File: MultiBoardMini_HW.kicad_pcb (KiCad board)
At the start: 2 copper layers, 63 x 63 mm, 57 parts, among them J1 PB0, J2 PA10, J3 Conn_01x02_Male, J4 PA10, J6 Conn_01x04, SW1 PF1, SW2 RESET, SW3 SW_Push_DPDT, SW5 SW_Push_DPDT, T3 PTS_1.5_2, U1 M78AR5-1, U2 NUCLEO-F303K8, U3 ESP32-C3-WROOM-02-N4, U4 TB67H303HG, U5 TB67H303HG, U6 MCP2562-E_SN

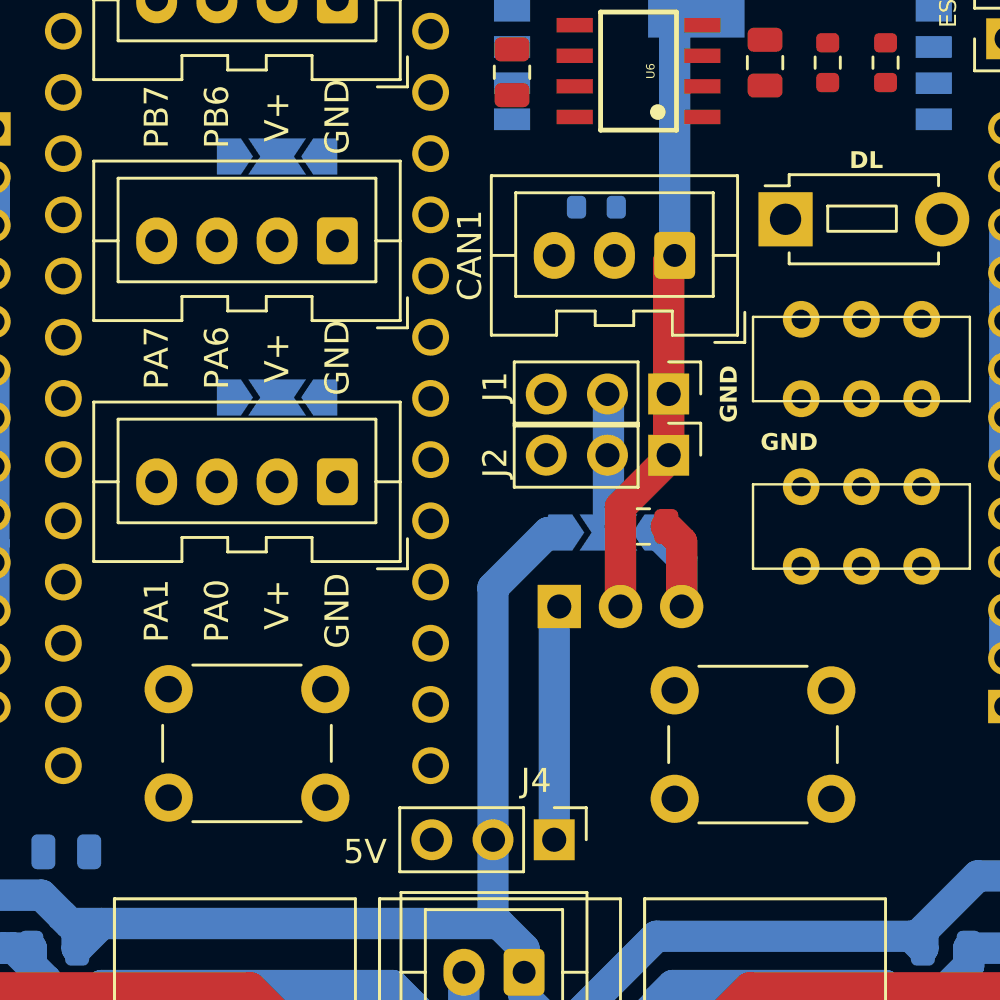
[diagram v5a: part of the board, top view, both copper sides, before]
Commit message: ESP大型化のためつめつめ
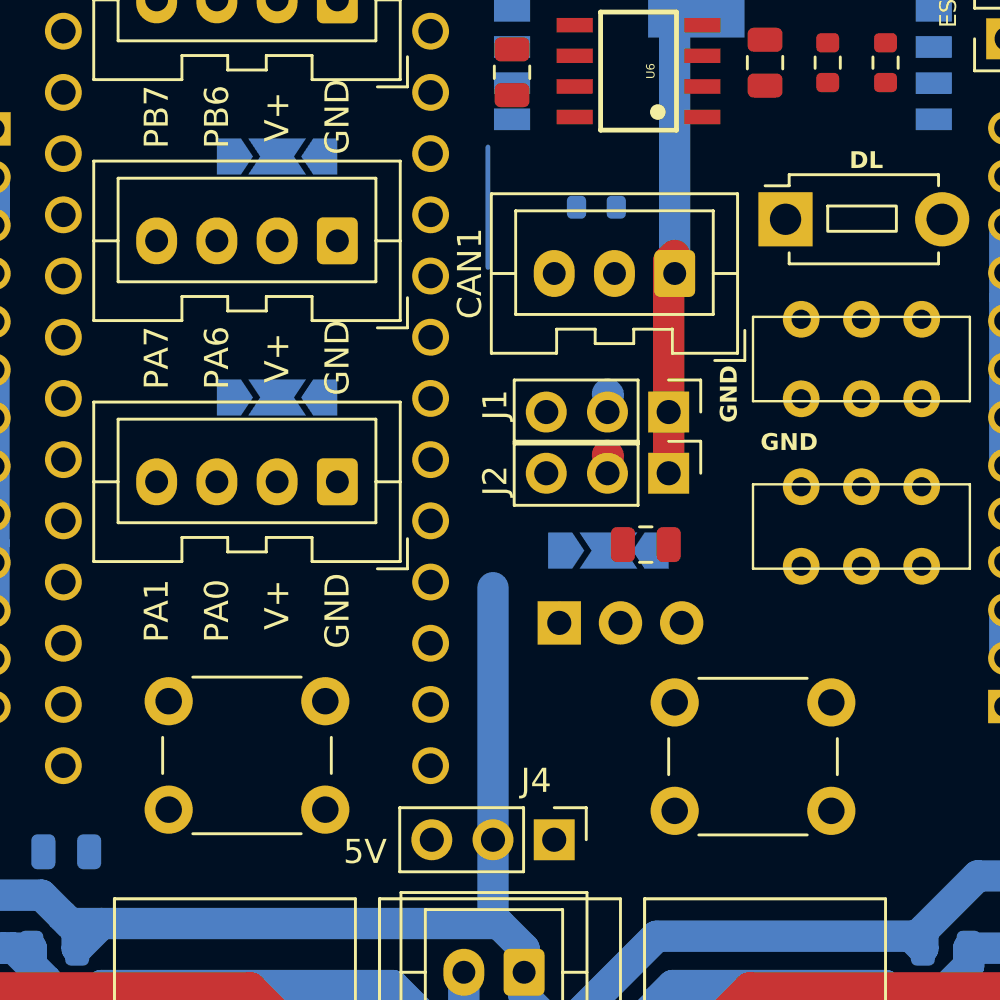
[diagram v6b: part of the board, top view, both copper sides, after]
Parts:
- moved C10 0.76 mm to (6.05, 5.75)
- moved CAN1 0.75 mm to (7.25, -5.50)
- moved J1 0.75 mm to (7.00, 0.25)
- moved J2 0.75 mm to (7.00, 2.79)
- moved JP4 0.75 mm to (4.50, 6.00)
- moved U1 0.68 mm to (5.00, 9.00)
- moved SW1 0.50 mm to (10.5, 14.5)
- moved SW2 0.50 mm to (-10.5, 14.5)
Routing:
- net Net-(J4-Pin_1): track 10.1 -> 0.30 mm
- net +5V: track 7.09 -> 0.00 mm
- net GND: track 182.2 -> 175.3 mm
- net Net-(J1-Pin_2): track 5.82 -> 0.11 mm
- net PWR: track 136.8 -> 133.0 mm
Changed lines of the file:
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@@
   )
   (footprint "Connector_PinHeader_2.54mm:PinHeader_1x03_P2.54mm_Vertical" (layer "F.Cu")
-    (at 7 -0.5 -90)
+    (at 7 0.25 -90)
     (descr "Through hole straight pin header, 1x03, 2.54mm pitch, single row")
     (tags "Through hole pin header THT 1x03 2.54mm single row")
@@
   )
   (footprint "Button_Switch_THT:SW_PUSH_6mm" (layer "F.Cu")
-    (at 10.5 14)
+    (at 10.5 14.5)
     (descr "https://www.omron.com/ecb/products/pdf/en-b3f.pdf")
     (tags "tact sw push 6mm")
@@
   )
   (footprint "Button_Switch_THT:SW_PUSH_6mm" (layer "F.Cu")
-    (at -10.5 14)
+    (at -10.5 14.5)
     (descr "https://www.omron.com/ecb/products/pdf/en-b3f.pdf")
     (tags "tact sw push 6mm")
@@
   )
   (footprint "Connector_JST:JST_XA_B03B-XASK-1_1x03_P2.50mm_Vertical" (layer "F.Cu")
-    (at 7.25 -6.25 180)
+    (at 7.25 -5.5 180)
     (descr "JST XA series connector, B03B-XASK-1 (http://www.jst-mfg.com/product/pdf/eng/eXA1.pdf), generated with kicad-footprint-generator")
     (tags "connector JST XA vertical")
@@
   )
   (footprint "Capacitor_SMD:C_0805_2012Metric" (layer "F.Cu")
-    (at 5.95 5 180)
+    (at 6.05 5.75 180)
     (descr "Capacitor SMD 0805 (2012 Metric), square (rectangular) end terminal, IPC_7351 nominal, (Body size source: IPC-SM-782 page 76, https://www.pcb-3d.com/wordpress/wp-content/uploads/ipc-sm-782a_amendment_1_and_2.pdf, https://docs.google.com/spreadsheets/d/1BsfQQcO9C6DZCsRaXUlFlo91Tg2WpOkGARC1WS5S8t0/edit?usp=sharing), generated with kicad-footprint-generator")
     (tags "capacitor")
@@
   )
   (footprint "Connector_PinHeader_2.54mm:PinHeader_1x03_P2.54mm_Vertical" (layer "F.Cu")
-    (at 7 2.04 -90)
+    (at 7 2.79 -90)
     (descr "Through hole straight pin header, 1x03, 2.54mm pitch, single row")
     (tags "Through hole pin header THT 1x03 2.54mm single row")
@@
   )
   (footprint "Jumper:SolderJumper-3_P2.0mm_Open_TrianglePad1.0x1.5mm" (layer "B.Cu")
-    (at 4.5 5.25)
+    (at 4.5 6)
     (descr "SMD Solder Jumper, 1x1.5mm Triangular Pads, 0.3mm gap, open")
     (tags "solder jumper open")
@@
   )
   (footprint "MultiBoardMini_Libraries:M78AR" (layer "B.Cu")
-    (at 5 8.32)
+    (at 5 9)
     (property "Sheetfile" "MultiBoardMini_HW.kicad_sch")
     (property "Sheetname" "")
@@
     )
   )
+  (gr_line (start -0.5 -10.75) (end -0.5 -5.75)
+    (stroke (width 0.2) (type default)) (layer "B.Cu"))
   (gr_line (start -1 29) (end -4 29)
     (stroke (width 0.3) (type default)) (layer "B.SilkS"))
@@
     (effects (font (size 1 1) (thickness 0.15)))
   )
-  (segment (start 7.54 5.64) (end 6.9 5) (width 1.3) (layer "F.Cu") (net 1))
-  (segment (start 7.54 8.32) (end 7.54 5.64) (width 1.3) (layer "F.Cu") (net 1))
-  (segment (start 6.5 5.25) (end 7.54 6.29) (width 1.3) (layer "B.Cu") (net 1))
-  (segment (start 7.54 6.29) (end 7.54 8.32) (width 1.3) (layer "B.Cu") (net 1))
   (segment (start 7 -0.5) (end 7 -6) (width 1.3) (layer "F.Cu") (net 2))
-  (segment (start 5 8.32) (end 5 5) (width 1.3) (layer "F.Cu") (net 2))
-  (segment (start 5 4.185358) (end 7 2.185358) (width 1.3) (layer "F.Cu") (net 2))
   (segment (start 7 -6) (end 7.25 -6.25) (width 1.3) (layer "F.Cu") (net 2))
-  (segment (start 5 5) (end 5 4.185358) (width 1.3) (layer "F.Cu") (net 2))
   (segment (start 7 2.185358) (end 7 -0.5) (width 1.3) (layer "F.Cu") (net 2))
   (segment (start 19.45 23.225) (end 19.45 22.5) (width 1.3) (layer "B.Cu") (net 2))
@@
   (segment (start -19.025 20.3) (end -18.1875 21.1375) (width 1.3) (layer "B.Cu") (net 4))
   (segment (start -19.025 20.3) (end -21.7 20.3) (width 1.3) (layer "B.Cu") (net 4))
-  (segment (start 2 5.25) (end -0.29 7.54) (width 1.3) (layer "B.Cu") (net 4))
   (segment (start 17.55 22.5) (end 17.55 21.775) (width 1.3) (layer "B.Cu") (net 4))
   (segment (start 1 24.5) (end 2.5 26) (width 1.3) (layer "B.Cu") (net 4))
@@
   (segment (start 19.825 19.5) (end 22.5 19.5) (width 1.3) (layer "B.Cu") (net 4))
   (segment (start -21.7 20.3) (end -22.5 19.5) (width 1.3) (layer "B.Cu") (net 4))
-  (segment (start 2.5 5.25) (end 2 5.25) (width 1.3) (layer "B.Cu") (net 4))
   (segment (start -18.1875 21.1375) (end -17.848753 21.476247) (width 1.3) (layer "B.Cu") (net 4))
   (segment (start 1 23.5) (end 1 22.525) (width 1.3) (layer "B.Cu") (net 4))
@@
   (segment (start -26.644 0.606) (end -26.644 -0.5) (width 1.3) (layer "F.Cu") (net 49))
   (segment (start 2.25 8.53) (end 2.46 8.32) (width 0.4) (layer "F.Cu") (net 66))
-  (segment (start 2.25 18) (end 2.25 8.53) (width 1.3) (layer "B.Cu") (net 66))
-  (segment (start 2.25 8.53) (end 2.46 8.32) (width 1.3) (layer "B.Cu") (net 66))
   (segment (start 4.5 2.08) (end 4.46 2.04) (width 1.3) (layer "F.Cu") (net 67))
-  (segment (start 4.5 5.25) (end 4.5 -0.46) (width 1.3) (layer "B.Cu") (net 67))
   (segment (start 4.5 -0.46) (end 4.46 -0.5) (width 1.3) (layer "B.Cu") (net 67))
   (zone (net 2) (net_name "GND") (layers "F&B.Cu") (hatch edge 0.5)

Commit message: toriaezu
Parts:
- removed U3: ESP32-C3-WROOM-02-N4, MultiBoardMini_Libraries:ESP-WROOM-02
- added U7: ESP32-WROOM-32, RF_Module:ESP32-WROOM-32, B.Cu at (9.25, -15.5)
- SW1, SW2: footprint Button_Switch_THT:SW_PUSH_6mm -> Button_Switch_SMD:SW_Push_1P1T_NO_6x6mm_H9.5mm
- SW3, SW5: footprint MultiBoardMini_Libraries:IS-2235 -> MultiBoardMini_Libraries:SSSS213202
- SW4: footprint Button_Switch_THT:SW_PUSH_1P1T_6x3.5mm_H4.3_APEM_MJTP1243 -> Button_Switch_SMD:SW_Push_1P1T_NO_Vertical_Wuerth_434133025816
- moved SW3 12.8 mm to (4.00, -8.50)
- moved R1 11.1 mm to (13.9, -3.25)
- moved SW4 10.7 mm to (3.50, -14.5)
- moved C2 10.7 mm to (10.0, -8.95)
- moved CAN1 10.5 mm to (16.6, -0.75)
- moved U6 9.69 mm to (14.2, -9.25), turned to -90 degrees
- moved C1 8.81 mm to (18.2, -9.25)
- moved R12 3.04 mm to (15.5, -17.2)
- moved R9 3.00 mm to (13.6, -17.2)
- moved JP4 2.62 mm to (3.70, 3.50)
- moved J1 2.41 mm to (6.25, -2.04)
- moved J2 2.41 mm to (6.25, 0.50)
- moved C10 2.26 mm to (6.25, 3.50)
- moved SW5 2.19 mm to (14.0, 6.95)
- moved U1 1.25 mm to (4.96, 7.75)
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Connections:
- U2 pad 3_1: Net-(J6-Pin_2) -> rx
- U2 pad 3_2: Net-(J6-Pin_1) -> tx
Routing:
- net GND: track 175.3 -> 155.3 mm
- net PWR: track 133.0 -> 122.6 mm

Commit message: 手動配線完成
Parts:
- added D2: D, Diode_SMD:D_SOD-123F, B.Cu at (6.20, 10.8)
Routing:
- net GND: track 155.3 -> 215.2 mm, vias 0 -> 2
- net +5V: track 0.00 -> 20.1 mm
- net PWR: track 122.6 -> 137.9 mm
- net Net-(U5-VREG): track 0.00 -> 11.4 mm, vias 0 -> 1
- net Net-(J4-Pin_1): track 0.00 -> 10.6 mm
- net +3V3: track 0.00 -> 7.48 mm
- net Net-(U4-VREG): track 0.00 -> 6.51 mm
- net Net-(J1-Pin_2): track 0.00 -> 5.54 mm
